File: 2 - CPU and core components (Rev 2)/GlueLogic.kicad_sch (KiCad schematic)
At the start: 31 parts, among them J1 READ INT MODE, U1 74HCT132, U2 74HCT74, U4 ATF22V10C, U5 ATF22V10C, U6 74HCT373, U7 74HCT273, U8 74HCT32, U9 74HCT373

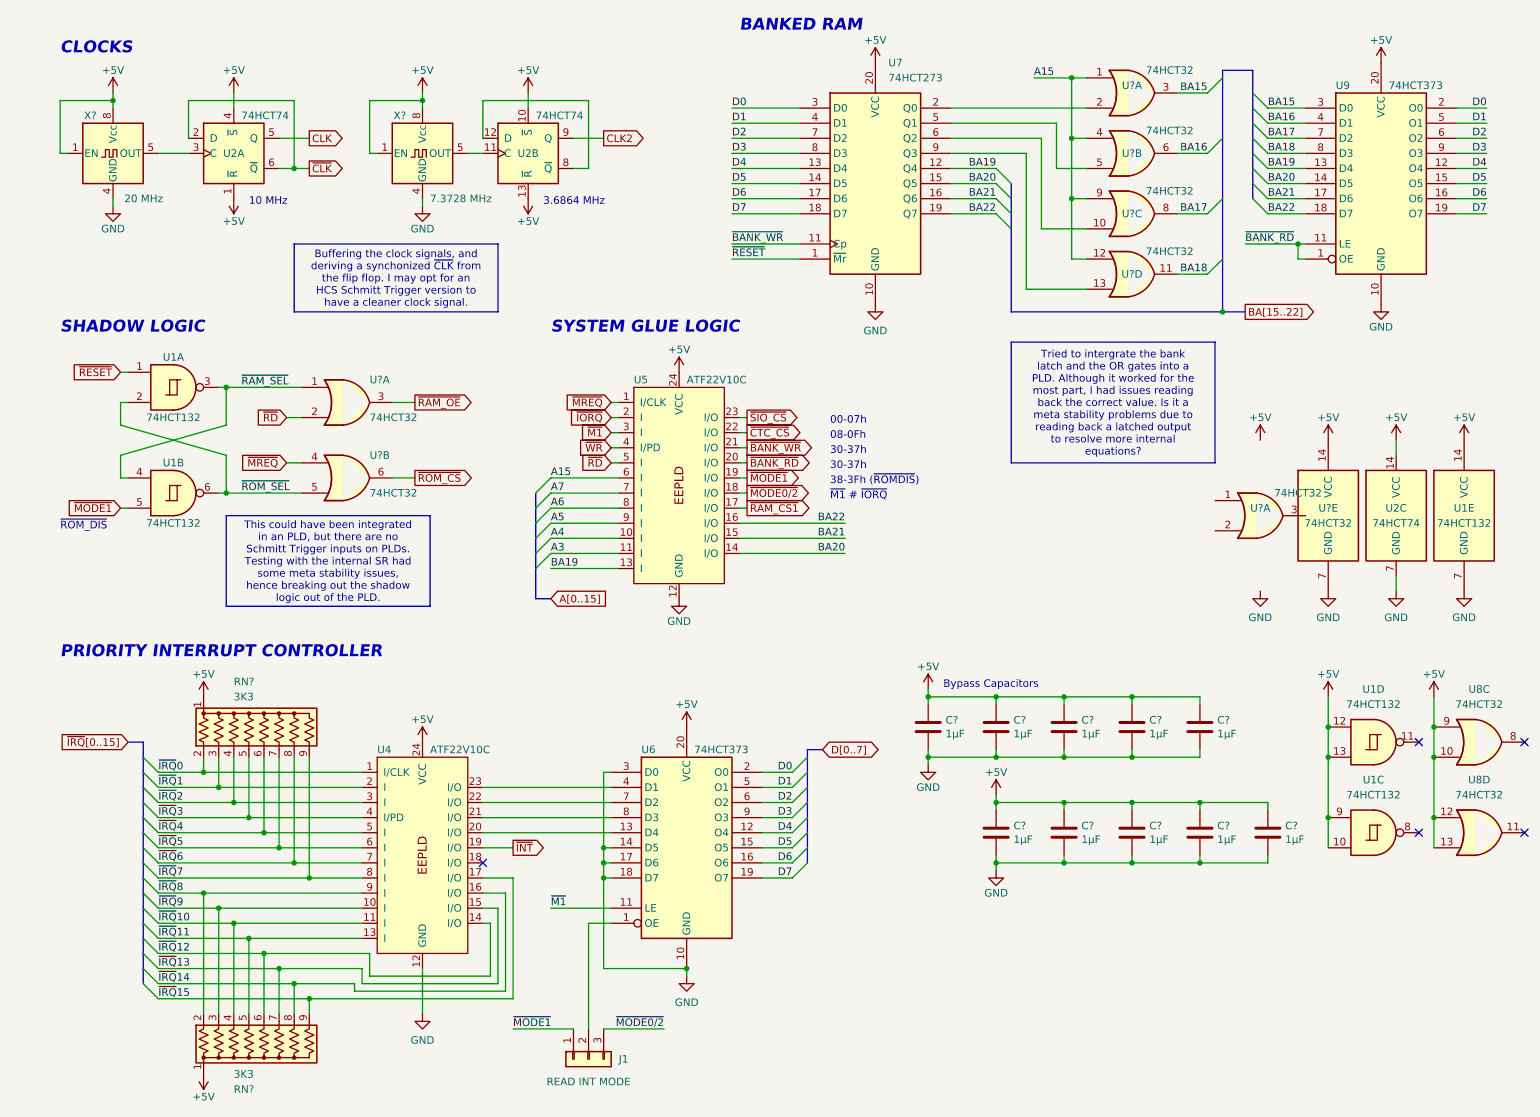
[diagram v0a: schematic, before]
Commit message: Added Interrupt Enable daisy chain jumpers between the ISA slots
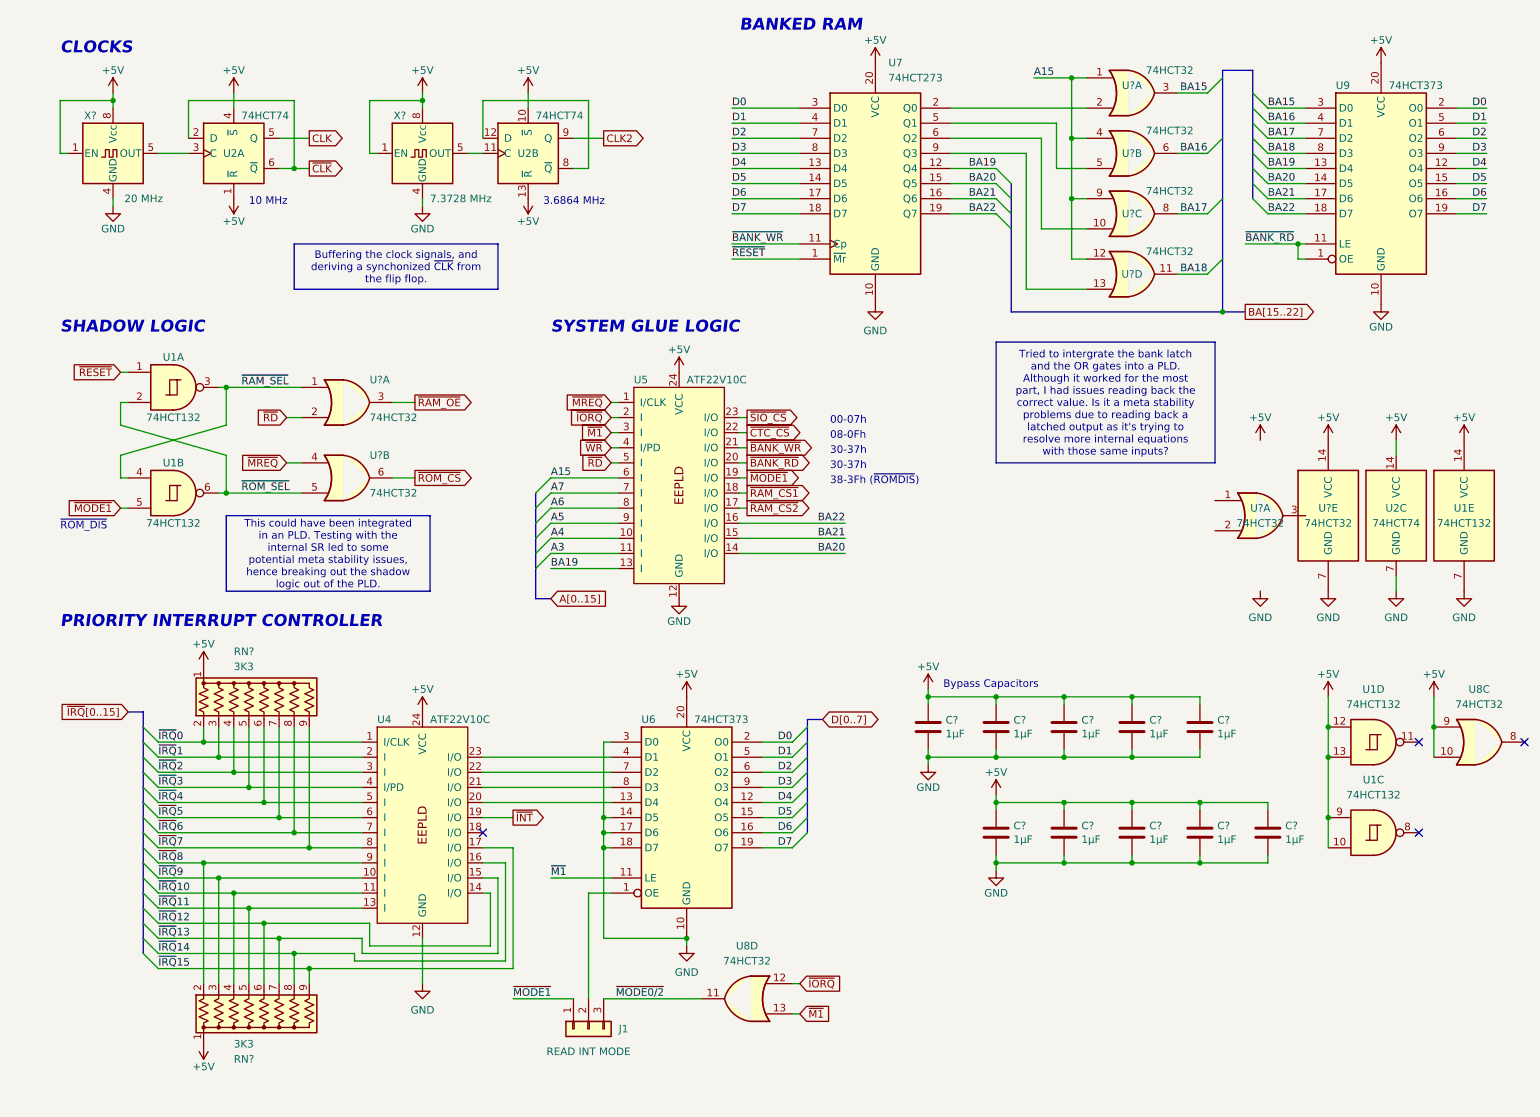
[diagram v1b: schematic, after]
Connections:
- net +5V: no longer U8.12, U8.13
- net ~{IORQ}: now also U8.12
- net ~{M1}: now also U8.13
- net ~{MODE0/2}: now also U8.11; no longer U5.18 (I/O)
- net ~{RAM_CS1}: now also U5.18 (I/O); no longer U5.17 (I/O)
- new net ~{RAM_CS2}: U5.17 (I/O)
- no-connect marks 5 -> 4
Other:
- note removed: "~{M1} # ~{IORQ}"
- title: (none) -> Glue Logic
- moved on the sheet: J1, RN?, U4, U6, U8D

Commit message: Finished component placement, currently routing.
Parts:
- removed C?: 1µF, Capacitor_THT:C_Disc_D3.0mm_W2.0mm_P2.50mm, symbol Device:C
- removed unit 3 of U1
- removed unit 4 of U1
- added C? (x2): 1µF, Capacitor_THT:C_Disc_D3.0mm_W2.0mm_P2.50mm, symbol Device:C
- J1: value READ INT MODE -> INT MODE
- U5: footprint Package_DIP:DIP-24_W7.62mm -> Package_DIP:DIP-24_W7.62mm_Socket
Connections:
- net +5V: now also C?.1, C?.1
- net A15: now also U5.11 (I); no longer U5.6 (I)
- net A3: now also U5.6 (I); no longer U5.11 (I)
- net A4: now also U5.7 (I); no longer U5.10 (I)
- net A5: now also U5.8 (I); no longer U5.9 (I)
- net A6: now also U5.9 (I); no longer U5.8 (I)
- net A7: now also U5.10 (I); no longer U5.7 (I)
- net GND: now also C?.2, C?.2
- net ~{IRQ}11: now also RN?.2 (R1); no longer RN?.5 (R4)
- net ~{IRQ}12: now also RN?.3 (R2); no longer RN?.6 (R5)
- net ~{IRQ}13: now also RN?.5 (R4); no longer RN?.7 (R6)
- net ~{IRQ}14: now also RN?.7 (R6); no longer RN?.8 (R7)
- net ~{IRQ}8: now also RN?.8 (R7); no longer RN?.2 (R1)
- net ~{IRQ}9: now also RN?.6 (R5); no longer RN?.3 (R2)
- net ~{RAM_CS1} renamed ~{RAM_CS}
- net ~{RAM_CS2}: no longer names the net of U5.17 (I/O)
- no-connect marks 4 -> 3
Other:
- moved on the sheet: C?, J1, RN?, U1E, U2C, U4, U6, U8C, U8D, U?A, U?E
